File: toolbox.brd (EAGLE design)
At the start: 100 x 80 mm, 73 parts, among them IC1 PIC18F4XK22PT, IC3 78L05SMD, T1 BC847, U2 AD654JRZ, U3 ADUM7441ARQZ

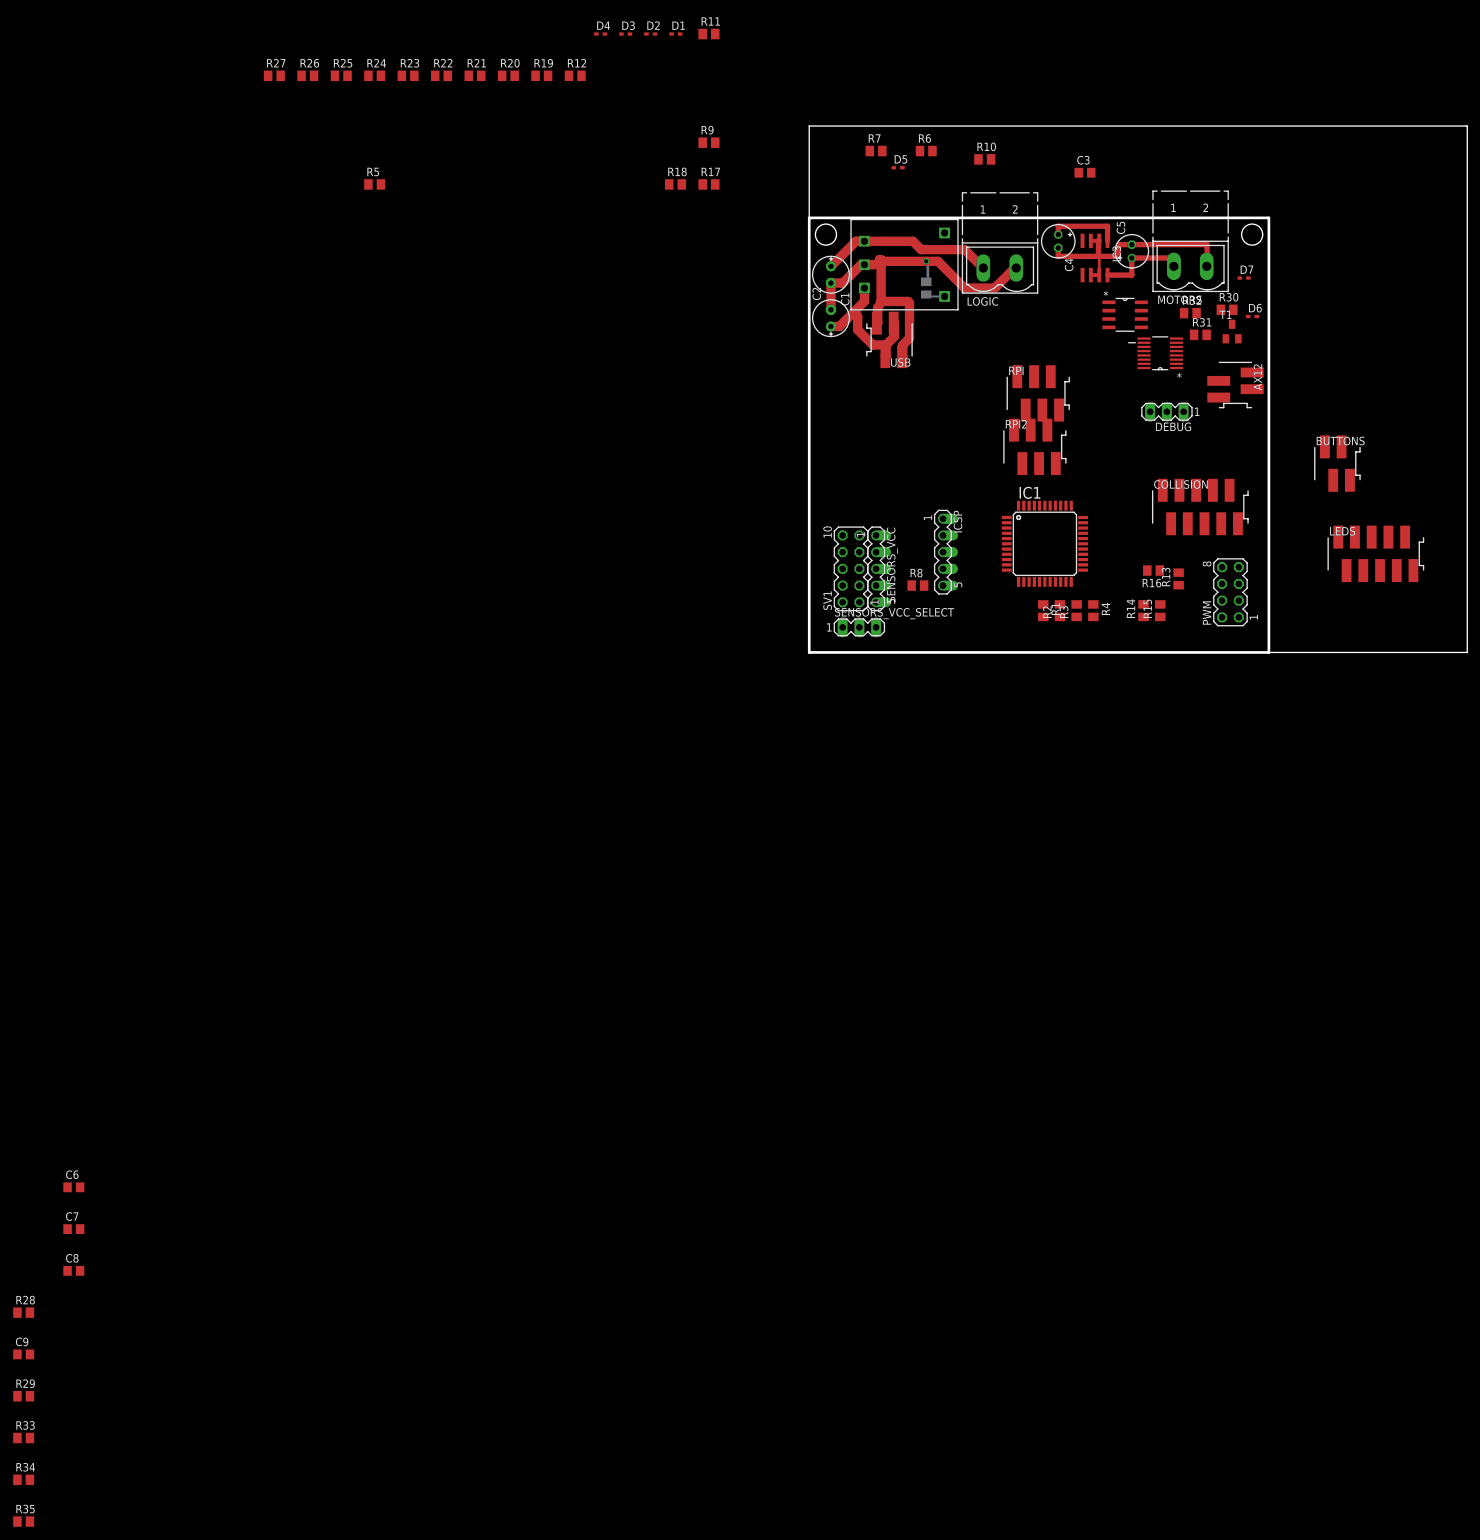
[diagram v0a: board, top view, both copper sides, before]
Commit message: WIP replaced AX-12 connector with 2x6pin micromatch routed motor side parts, sensor, buttons and LEDs connectors
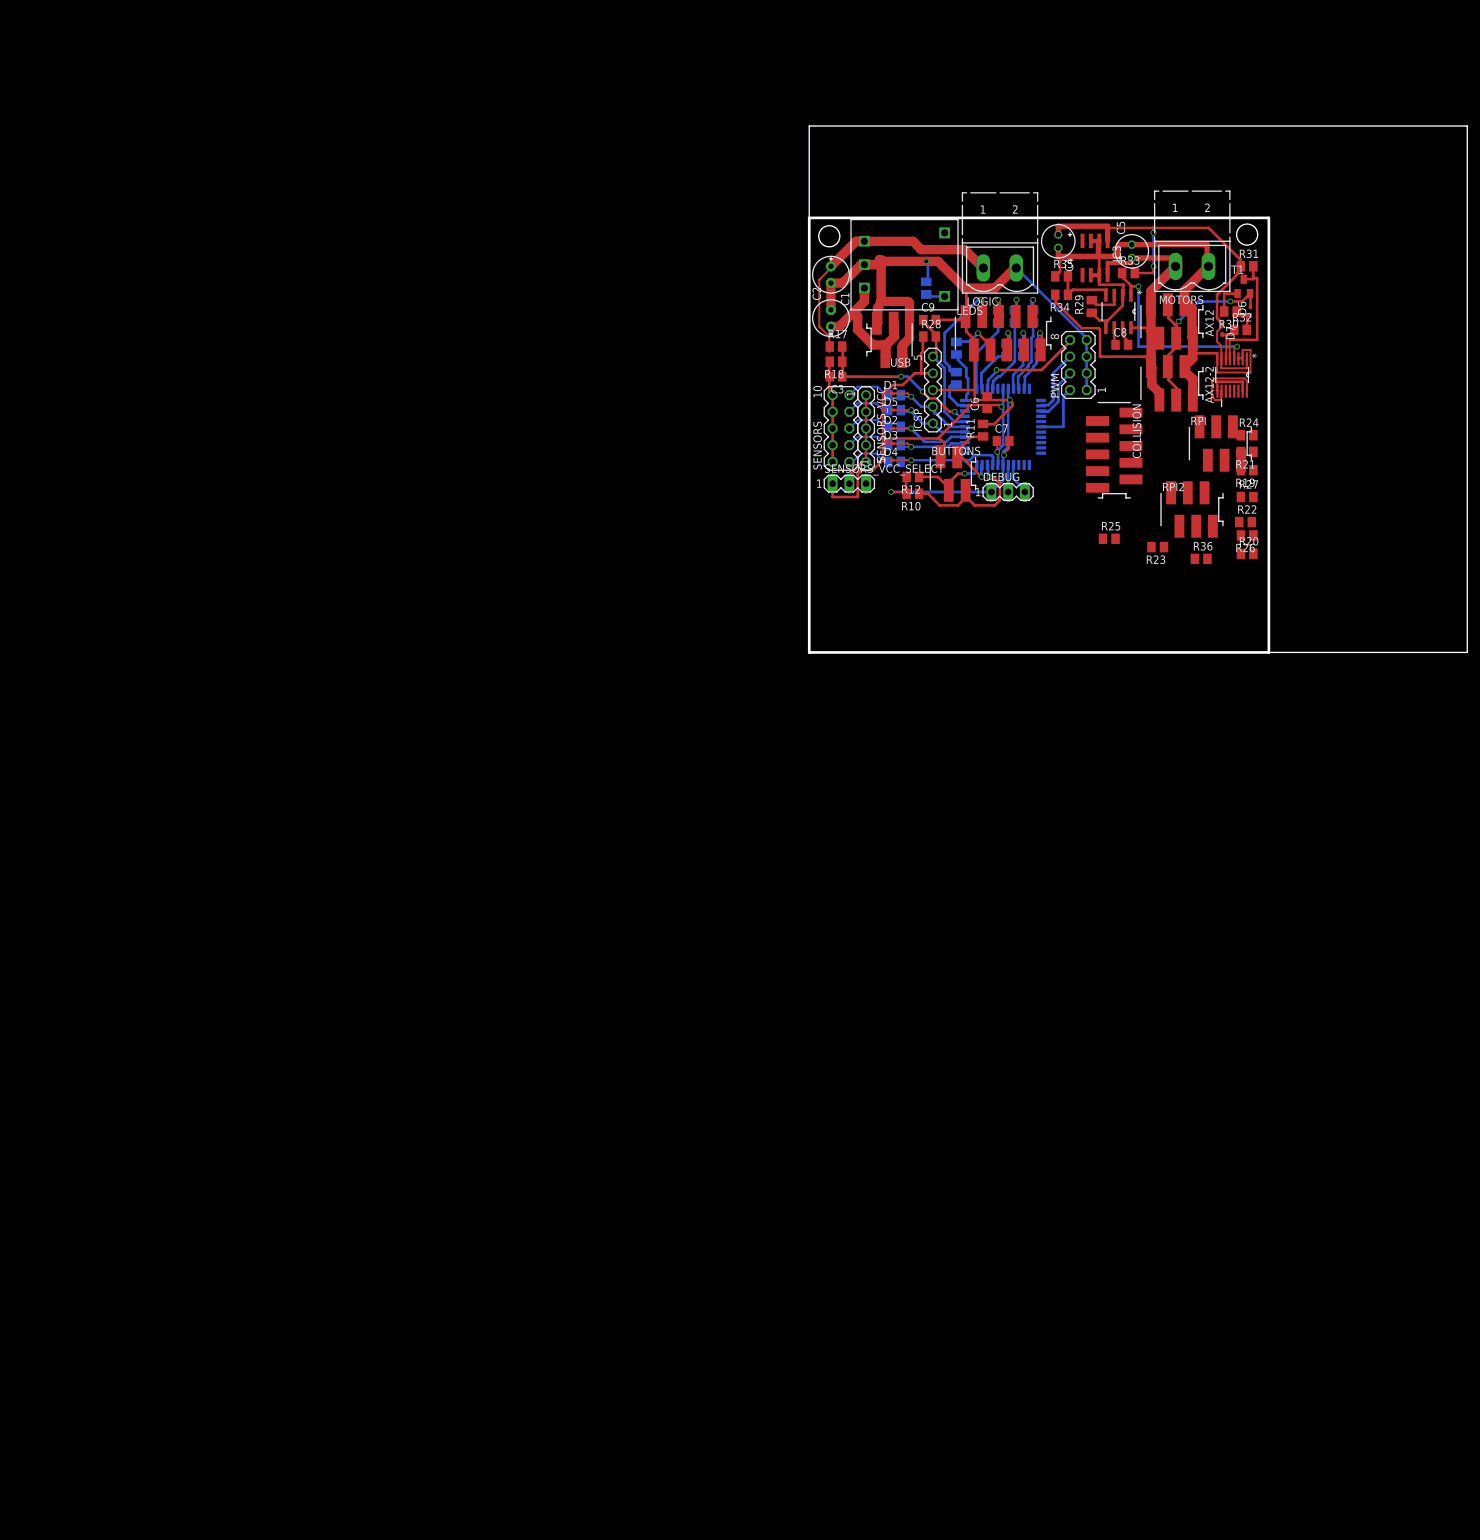
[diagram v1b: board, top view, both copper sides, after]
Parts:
- removed SV1: (no value), con-lstb:MA05-2
- added AX12-2: (no value), con-amp:SMDTOP6
- added R36: 22k, rcl:M0805
- added SENSORS: (no value), con-lstb:MA05-2
- AX12: device con-amp:SMDTOP4 -> con-amp:SMDTOP6
- R10, R11, R12, R19, R20, R21, R22, R23, R24, R25, R26, R27: value (none) -> 22k
- moved R35 246.3 mm to (38.4, 57.1)
- moved R33 244.0 mm to (48.5, 57.7)
- moved R34 239.4 mm to (38.4, 54.4), turned to 180 degrees
- moved R29 231.9 mm to (42.9, 52.6), turned to 90 degrees
- moved C8 212.5 mm to (47.5, 46.7)
- moved C9 209.0 mm to (18.3, 50.5)
- moved R28 202.4 mm to (18.3, 48.0)
- moved C7 185.2 mm to (29.5, 32.1)
- moved C6 183.0 mm to (27.1, 38.0), turned to 90 degrees
- moved R27 161.1 mm to (66.5, 23.6)
- moved R26 158.9 mm to (66.5, 17.8), turned to 180 degrees
- moved R24 143.4 mm to (66.5, 33.0)
- moved R22 139.7 mm to (66.3, 19.8)
- moved R25 136.3 mm to (45.6, 17.3)
- moved R23 134.6 mm to (53.0, 16.0), turned to 180 degrees
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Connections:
- new net N$57: IC1.27, U3.13
- net GND: now also SENSORS.10, SENSORS.2, SENSORS.4, SENSORS.6, SENSORS.8; no longer SV1.10, SV1.2, SV1.4, SV1.6, SV1.8
- net N$11: now also SENSORS.9; no longer SV1.9
- net N$12: now also SENSORS.7; no longer SV1.7
- net N$13: now also SENSORS.5; no longer SV1.5
- net N$14: now also SENSORS.3; no longer SV1.3
- net N$15: now also SENSORS.1; no longer SV1.1
- net N$27: now also R15.2; no longer R13.2
- net N$29: now also IC1.32, R16.2; no longer IC1.27, R15.2
- net N$30: now also R13.2; no longer R16.2
- net N$39: now also IC1.19; no longer IC1.20
- net N$44: no longer R22.1
- net N$45: now also R22.1, R36.2
- net N$46: now also PWM.4; no longer PWM.8
- net N$47: now also PWM.8; no longer PWM.2
- net N$48: now also PWM.2; no longer PWM.4
- net N$52: now also AX12-2.3, AX12-2.4, AX12.4
- net N$61: now also AX12-2.1, AX12-2.2, AX12.1
- net N$67: now also AX12-2.5, AX12-2.6, AX12.5, AX12.6, U3.3; no longer AX12.4
- net VCC: now also R36.1
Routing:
- net GND: track 64.4 -> 191.6 mm, vias 1 -> 4
- net VCC: track 0.00 -> 91.7 mm, vias 0 -> 2
- net N$67: track 39.2 -> 100.7 mm
- net N$68: track 11.0 -> 67.6 mm, vias 0 -> 2
- net N$61: track 13.9 -> 62.9 mm
- net N$52: track 0.00 -> 32.0 mm, vias 0 -> 2
- net N$63: track 0.00 -> 31.5 mm, vias 0 -> 2
- net N$39: track 0.00 -> 26.6 mm, vias 0 -> 3
- net N$24: track 0.00 -> 24.2 mm, vias 0 -> 1
- net N$55: track 0.00 -> 20.5 mm
- net N$3: track 0.00 -> 19.6 mm
- net N$18: track 0.00 -> 19.3 mm, vias 0 -> 1
- net N$10: track 0.00 -> 17.8 mm, vias 0 -> 1
- net N$47: track 0.00 -> 16.7 mm, vias 0 -> 1
- net N$1: track 0.00 -> 15.9 mm, vias 0 -> 1
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
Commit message: WIP finished routing the board Removed useless datasheet
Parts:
- added C10, C11: 100n, rcl:C0805
- moved R19 33.1 mm to (41.8, 5.59), flipped to the bottom, turned to 0 degrees
- moved R21 31.7 mm to (41.8, 10.7), flipped to the bottom, turned to 0 degrees
- moved R24 27.0 mm to (46.9, 14.5), flipped to the bottom
- moved R27 25.8 mm to (46.9, 6.86), flipped to the bottom
- moved R20 25.6 mm to (41.8, 8.13), flipped to the bottom
- moved R22 24.8 mm to (41.8, 15.7), flipped to the bottom
- moved RPI 23.7 mm to (54.5, 9.40), turned to 90 degrees
- moved R26 21.3 mm to (46.9, 9.40), flipped to the bottom, turned to 0 degrees
- moved C1 21.3 mm to (3.37, 36.1)
- moved IC3 21.3 mm to (43.5, 38.6)
- moved AX12 21.3 mm to (55.2, 29.0)
- moved D2 21.3 mm to (12.0, 12.7)
- moved D4 21.3 mm to (12.0, 7.87)
- moved D6 21.3 mm to (67.1, 30.5)
- moved LEDS 21.3 mm to (29.5, 27.2)
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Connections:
- net GND: now also C10.2
- net N$67: now also C11.2
- net N$68: now also C11.1
- net VCC: now also C10.1
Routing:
- net GND: track 191.6 -> 264.1 mm, vias 4 -> 7
- net VCC: track 91.7 -> 158.5 mm, vias 2 -> 4
- net VDD: track 0.00 -> 66.0 mm
- net N$35: track 41.5 -> 90.1 mm, vias 0 -> 1
- net N$57: track 0.00 -> 41.6 mm, vias 0 -> 3
- net N$7: track 0.00 -> 40.7 mm, vias 0 -> 1
- net N$54: track 0.00 -> 40.4 mm, vias 0 -> 1
- net N$56: track 0.00 -> 37.8 mm, vias 0 -> 1
- net N$9: track 0.00 -> 35.4 mm, vias 0 -> 1
- net N$41: track 0.00 -> 34.2 mm, vias 0 -> 3
- net N$8: track 0.00 -> 33.8 mm, vias 0 -> 1
- net N$43: track 0.00 -> 22.9 mm, vias 0 -> 2
- net N$45: track 0.00 -> 20.9 mm, vias 0 -> 1
- net N$42: track 0.00 -> 19.8 mm, vias 0 -> 2
- net N$48: track 9.35 -> 24.6 mm
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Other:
- board size 100 x 80 mm -> 69.8 x 45 mm
- board text added: "3V3"
- board text added: "5V"

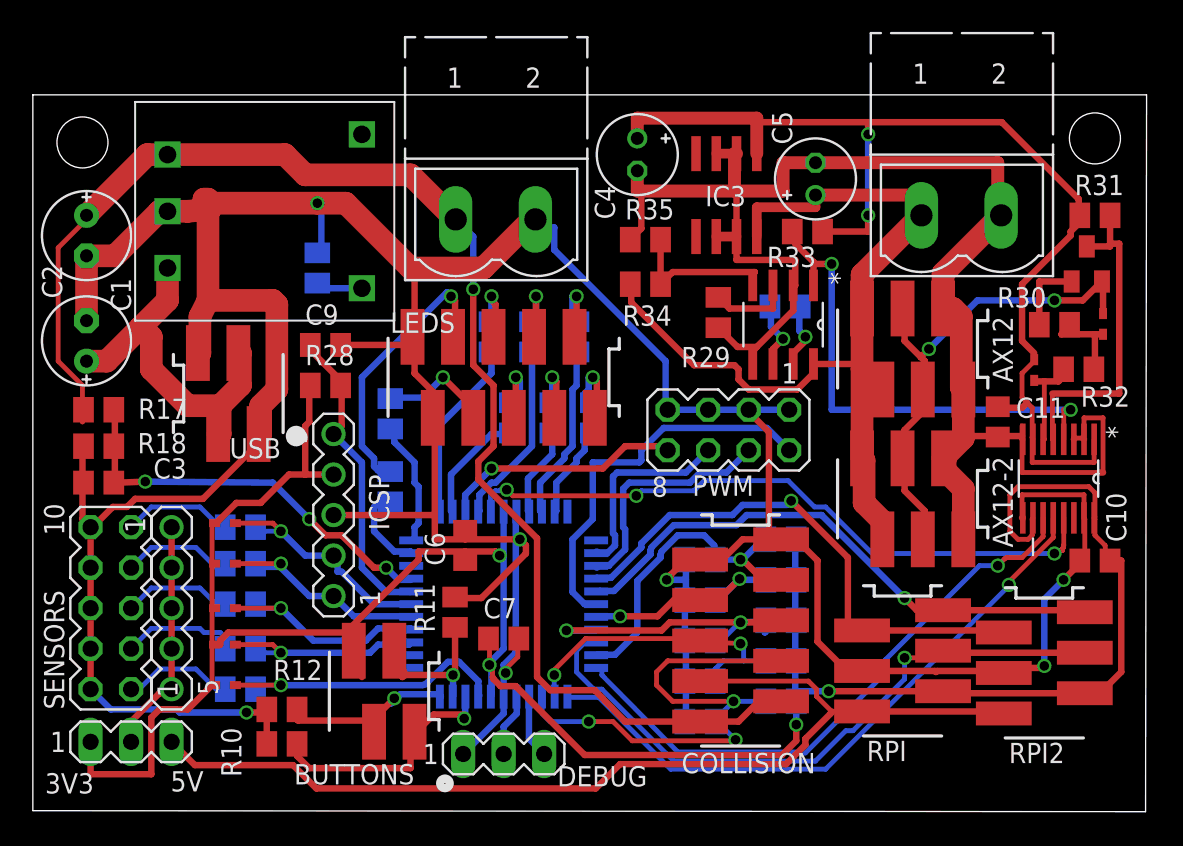
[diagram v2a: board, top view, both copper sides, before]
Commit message: moved labels and created ground planes with vias between them
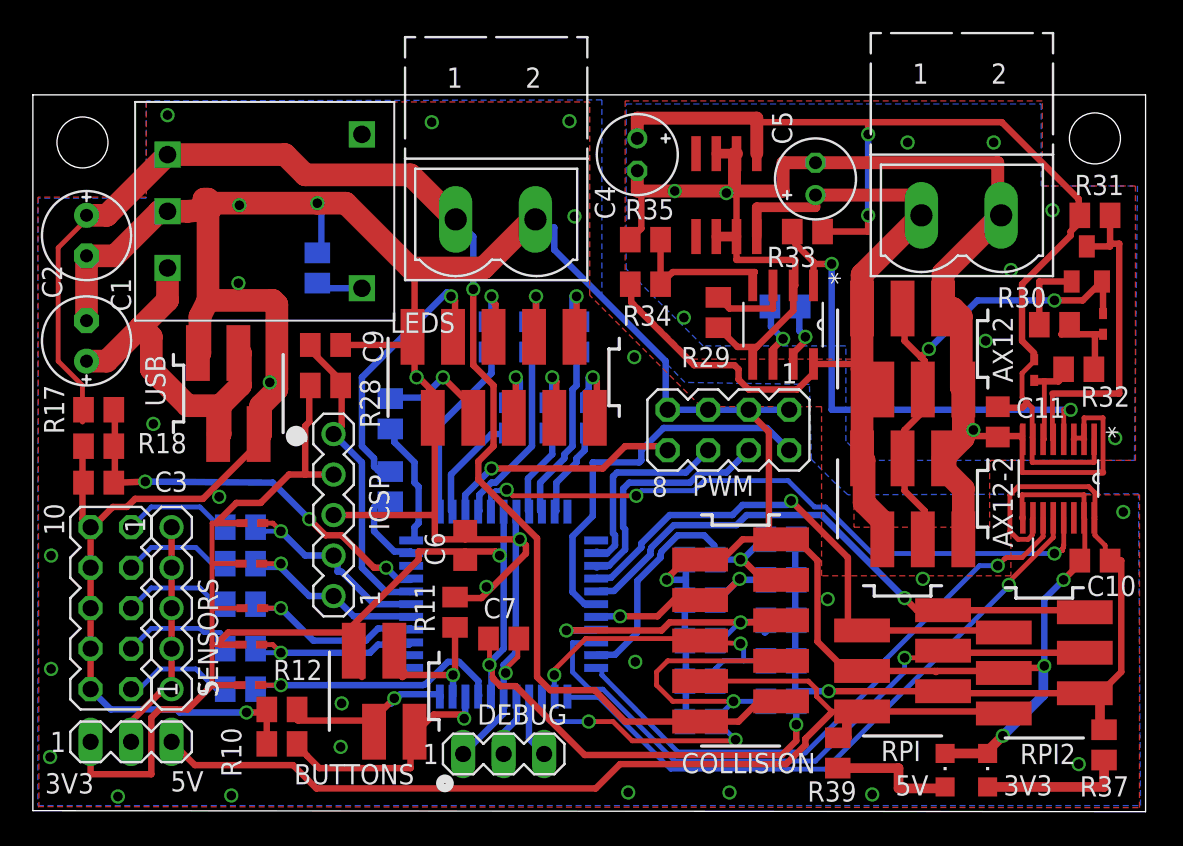
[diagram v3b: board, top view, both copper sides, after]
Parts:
- added 3V3, 5V: (no value), adafruit:CHIPLED_0805
- added R37, R39: 4.7k, rcl:M0805
- moved D1 1.71 mm to (13.7, 18.0)
- moved D2 1.71 mm to (13.7, 12.7)
- moved D3 1.65 mm to (13.7, 10.4)
- moved D5 1.65 mm to (13.7, 15.5)
- moved D4 1.59 mm to (13.6, 7.87)
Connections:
- net N$67 renamed GND_MOTOR
- new net N$60: 3V3.A, R37.2
- new net N$64: 5V.A, R39.2
- net GND: now also 3V3.C, 5V.C
- net VCC: now also R37.1
- net VDD: now also R39.1
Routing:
- net VCC: track 158.5 -> 171.8 mm
- net GND: track 264.1 -> 273.7 mm, vias 7 -> 35
- net N$60: track 0.00 -> 8.99 mm
- net N$64: track 0.00 -> 8.10 mm
- net VDD: track 66.0 -> 68.2 mm
- net N$16: track 14.3 -> 12.6 mm
- net N$1: track 15.9 -> 14.1 mm
- net N$17: track 13.8 -> 12.1 mm
- net N$2: track 14.6 -> 13.0 mm
- net N$18: track 19.7 -> 18.1 mm
- net N$7: track 40.7 -> 41.2 mm
- net GND_MOTOR: vias 0 -> 10
- added copper zone on layer 1, net GND
- added copper zone on layer 16, net GND
- added copper zone on layer 1, net GND_MOTOR
- added copper zone on layer 16, net GND_MOTOR
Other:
- board text added: "(c) 2016"
- board text added: "Telecom Robotics"
- board text added: "Toolbox board v1.0"
